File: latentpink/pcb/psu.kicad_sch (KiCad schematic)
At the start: 113 parts, among them J13 CONN_01X05, J14 CONN_01X03, J6 BARREL_JACK, U10 MYMGK1R812ERSR, U11 MYMGK00504ERSR, U12 STM32L031-QFN32, U13 MYMGK00504ERSR, U14 MYMGK00504ERSR, U15 MYMGK00504ERSR, U16 NCP45521IMNTWG-H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

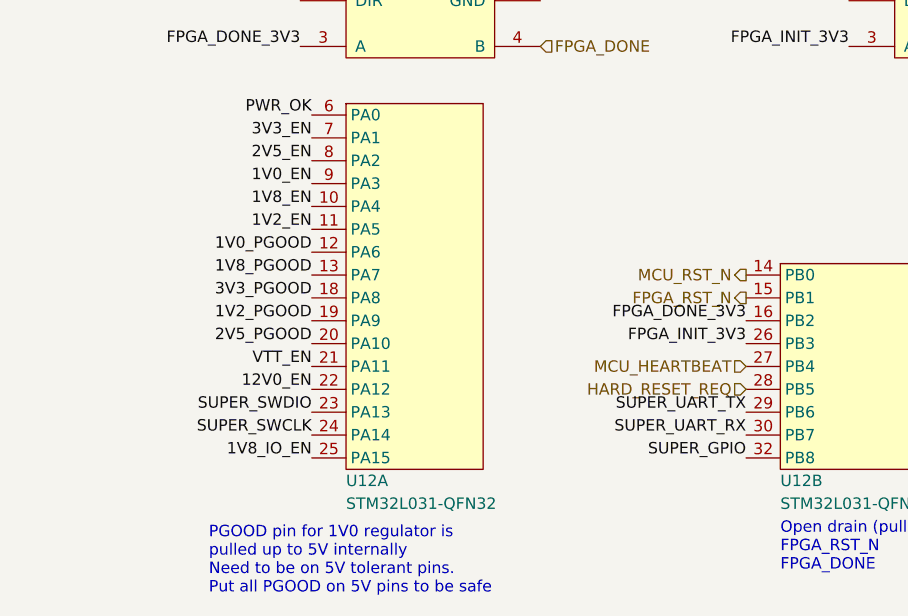
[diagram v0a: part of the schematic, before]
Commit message: Lots more layout of low speed stuff and power. Partial layout of 1.2V supply. Initial RGMII escape routing.
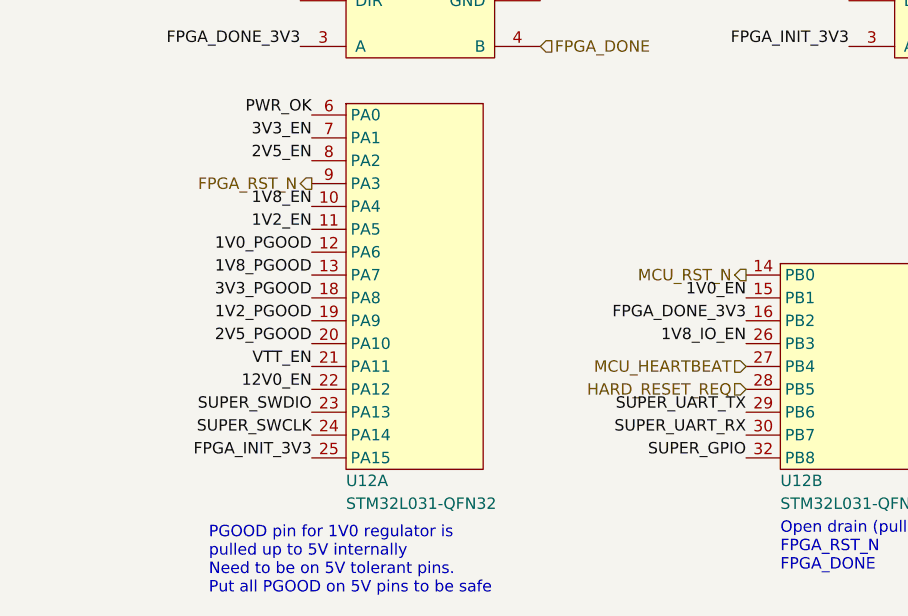
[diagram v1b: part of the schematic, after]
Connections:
- net 1V0_EN: now also U12.15 (PB1); no longer U12.9 (PA3)
- net 1V8_IO_EN: now also U12.26 (PB3); no longer U12.25 (PA15)
- net FPGA_INIT_3V3: now also U12.25 (PA15); no longer U12.26 (PB3)
- net FPGA_RST_N: now also U12.9 (PA3); no longer U12.15 (PB1)
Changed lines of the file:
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@@
   (paper "A3")
   (title_block
-    (date "2023-05-31")
+    (date "2023-06-01")
     (rev "0.1")
     (company "Antikernel Labs")
@@
     (effects (font (size 1.27 1.27)) (justify right bottom))
   )
-  (label "FPGA_INIT_3V3" (at 101.6 250.19 180)
+  (label "FPGA_INIT_3V3" (at 53.34 262.89 180)
     (effects (font (size 1.27 1.27)) (justify right bottom))
   )
@@
     (effects (font (size 1.27 1.27)) (justify right bottom))
   )
-  (label "1V8_IO_EN" (at 53.34 262.89 180)
+  (label "1V8_IO_EN" (at 101.6 250.19 180)
     (effects (font (size 1.27 1.27)) (justify right bottom))
   )
@@
     (effects (font (size 1.27 1.27)) (justify left bottom))
   )
-  (label "1V0_EN" (at 53.34 232.41 180)
+  (label "1V0_EN" (at 101.6 245.11 180)
     (effects (font (size 1.27 1.27)) (justify right bottom))
   )
@@
     (effects (font (size 1.27 1.27)) (justify left))
   )
-  (hierarchical_label "FPGA_RST_N" (shape output) (at 101.6 245.11 180)
+  (hierarchical_label "FPGA_RST_N" (shape output) (at 53.34 232.41 180)
     (effects (font (size 1.27 1.27)) (justify right))
   )

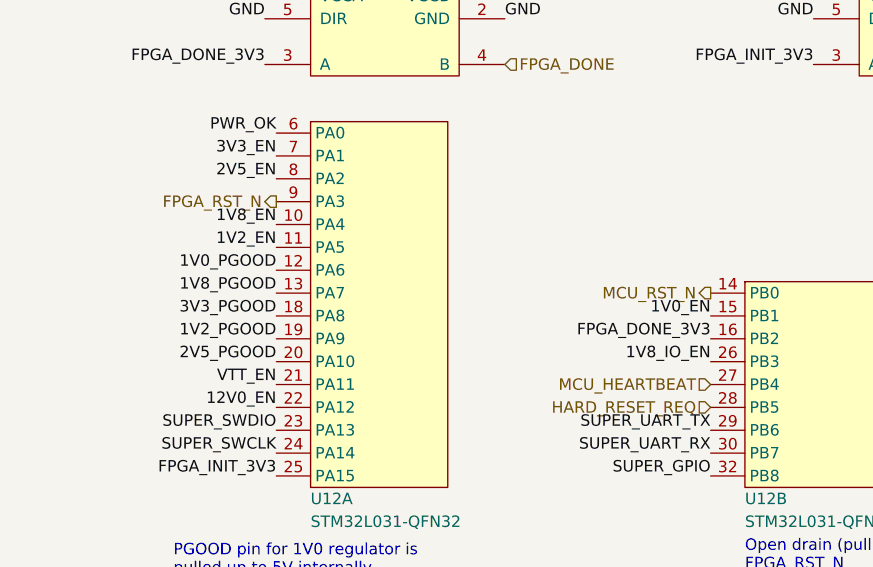
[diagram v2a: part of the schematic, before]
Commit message: Finished initial QDR routing, not length matched. 74 unrouted.
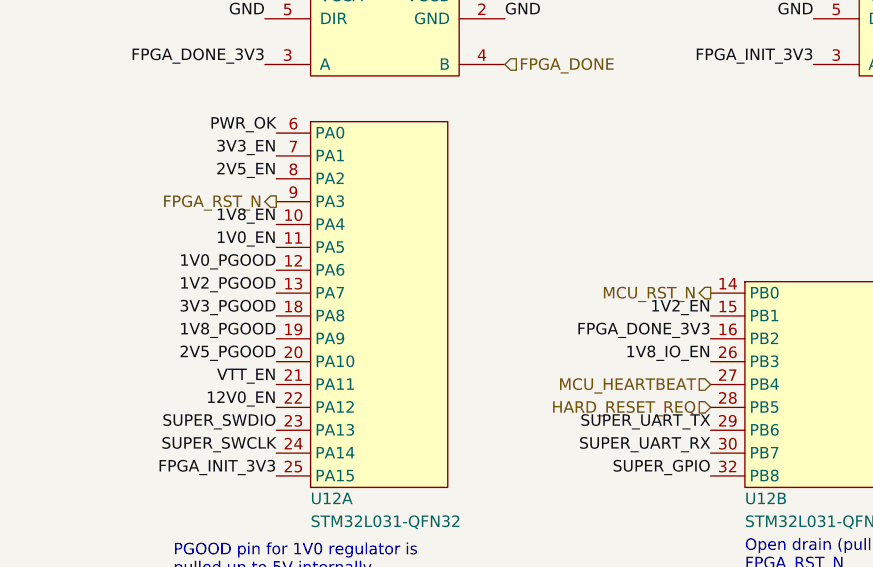
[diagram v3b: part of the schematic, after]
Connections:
- net 1V0_EN: now also U12.11 (PA5); no longer U12.15 (PB1)
- net 1V2_EN: now also U12.15 (PB1); no longer U12.11 (PA5)
- net 1V2_PGOOD: now also U12.13 (PA7); no longer U12.19 (PA9)
- net 1V8_PGOOD: now also U12.19 (PA9); no longer U12.13 (PA7)
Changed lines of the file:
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@@
     (effects (font (size 1.27 1.27)) (justify left bottom))
   )
-  (label "1V2_EN" (at 53.34 237.49 180)
+  (label "1V2_EN" (at 101.6 245.11 180)
     (effects (font (size 1.27 1.27)) (justify right bottom))
   )
@@
     (effects (font (size 1.27 1.27)) (justify left bottom))
   )
-  (label "1V8_PGOOD" (at 53.34 242.57 180)
+  (label "1V8_PGOOD" (at 53.34 247.65 180)
     (effects (font (size 1.27 1.27)) (justify right bottom))
   )
@@
     (effects (font (size 1.27 1.27)) (justify left bottom))
   )
-  (label "1V0_EN" (at 101.6 245.11 180)
+  (label "1V0_EN" (at 53.34 237.49 180)
     (effects (font (size 1.27 1.27)) (justify right bottom))
   )
@@
     (effects (font (size 1.27 1.27)) (justify right bottom))
   )
-  (label "1V2_PGOOD" (at 53.34 247.65 180)
-    (effects (font (size 1.27 1.27)) (justify right bottom))
-  )
+  (label "1V2_PGOOD" (at 53.34 242.57 180)
+    (effects (font (size 1.27 1.27)) (justify right bottom))
+  )

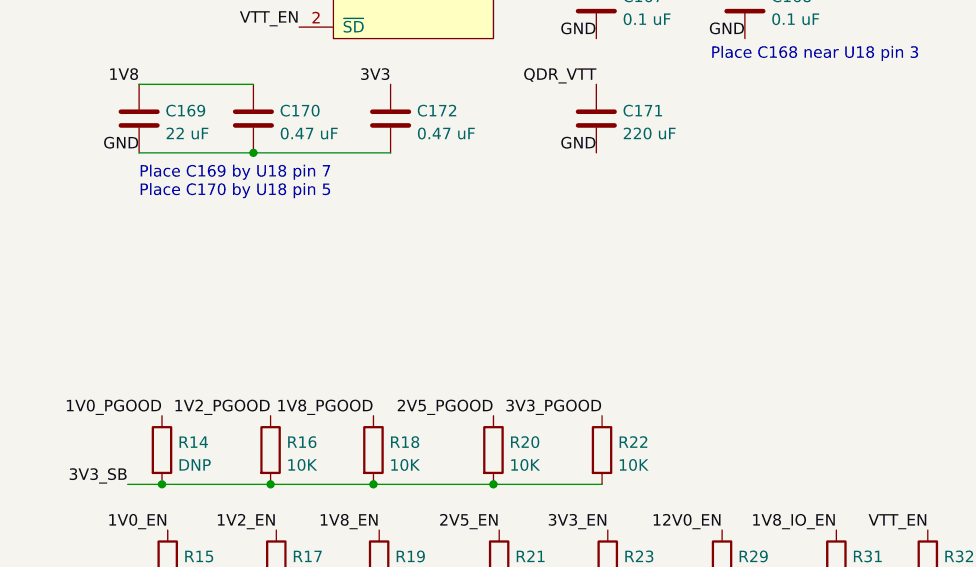
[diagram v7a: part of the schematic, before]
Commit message: Updated schematic with notes on power rail sequencing bug found during bringup
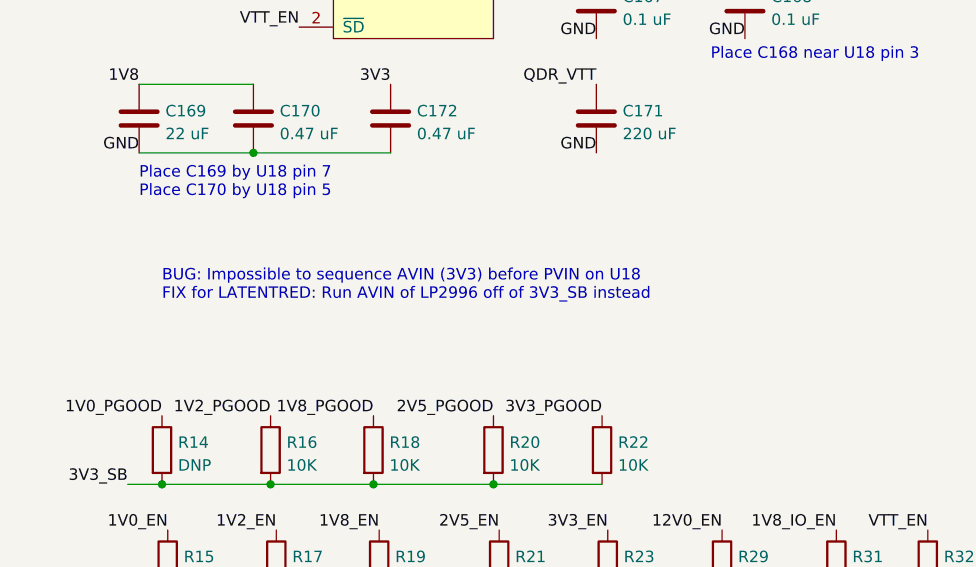
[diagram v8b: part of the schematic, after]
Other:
- note added: "BUG: Impossible to sequence AVIN (3V3) before PVIN on U18 FIX for LATENTRED: Run AVIN of LP2996 off of 3V3_SB instead"
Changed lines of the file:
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@@
+    (effects (font (size 1.27 1.27)) (justify left bottom))
+  )
+  (text "BUG: Impossible to sequence AVIN (3V3) before PVIN on U18\nFIX for LATENTRED: Run AVIN of LP2996 off of 3V3_SB instead"
+    (at 312.42 213.36 0)
     (effects (font (size 1.27 1.27)) (justify left bottom))
   )
@@
       (effects (font (size 1.27 1.27)) hide)
     )
-    (pin "10")
-    (pin "11")
-    (pin "12")
-    (pin "13")
-    (pin "18")
-    (pin "19")
-    (pin "20")
-    (pin "21")
-    (pin "22")
-    (pin "23")
-    (pin "24")
-    (pin "25")
-    (pin "6")
-    (pin "7")
-    (pin "8")
-    (pin "9")
-    (pin "14")
-    (pin "15")
-    (pin "16")
-    (pin "26")
-    (pin "27")
-    (pin "28")
-    (pin "29")
-    (pin "30")
-    (pin "32")
-    (pin "2")
-    (pin "3")
     (pin "1")
     (pin "17")
@@
       (effects (font (size 1.27 1.27)) hide)
     )
-    (pin "10")
-    (pin "11")
-    (pin "12")
-    (pin "13")
-    (pin "18")
-    (pin "19")
-    (pin "20")
-    (pin "21")
-    (pin "22")
-    (pin "23")
-    (pin "24")
-    (pin "25")
-    (pin "6")
-    (pin "7")
-    (pin "8")
-    (pin "9")
     (pin "14")
     (pin "15")
@@
     (pin "30")
     (pin "32")
-    (pin "2")
-    (pin "3")
-    (pin "1")
-    (pin "17")
-    (pin "31")
-    (pin "4")
-    (pin "5")
-    (pin "PAD")
   )
   (symbol (lib_id "passive-azonenberg:R_PWR") (at 120.65 45.72 270) (unit 1)
@@
     (pin "8")
     (pin "9")
-    (pin "14")
-    (pin "15")
-    (pin "16")
-    (pin "26")
-    (pin "27")
-    (pin "28")
-    (pin "29")
-    (pin "30")
-    (pin "32")
-    (pin "2")
-    (pin "3")
-    (pin "1")
-    (pin "17")
-    (pin "31")
-    (pin "4")
-    (pin "5")
-    (pin "PAD")
   )
   (symbol (lib_id "device:R") (at 335.915 229.87 0) (unit 1)
@@
       (effects (font (size 1.27 1.27)) hide)
     )
-    (pin "10")
-    (pin "11")
-    (pin "12")
-    (pin "13")
-    (pin "18")
-    (pin "19")
-    (pin "20")
-    (pin "21")
-    (pin "22")
-    (pin "23")
-    (pin "24")
-    (pin "25")
-    (pin "6")
-    (pin "7")
-    (pin "8")
-    (pin "9")
-    (pin "14")
-    (pin "15")
-    (pin "16")
-    (pin "26")
-    (pin "27")
-    (pin "28")
-    (pin "29")
-    (pin "30")
-    (pin "32")
     (pin "2")
     (pin "3")
-    (pin "1")
-    (pin "17")
-    (pin "31")
-    (pin "4")
-    (pin "5")
-    (pin "PAD")
   )
   (symbol (lib_id "device:C") (at 337.82 193.04 0) (unit 1)
